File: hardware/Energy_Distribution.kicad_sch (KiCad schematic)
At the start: 22 parts, among them J15 53398-0271, J16 53398-0671, J17 53398-0671, J18 53398-0271, U17 NVTFS5116PLTAG, U18 NVTFS5116PLTAG, U21 LMV321RIYLT, U39 NVTFS5116PLTAG, U4 INA199C1DCKR, U40 NVTFS5116PLTAG

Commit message: commit
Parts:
- removed R32: 110k, symbol Device:R_US
- removed R33, R35: 0.0R, symbol Device:R_US
- removed R34: 37.4k, symbol Device:R_US
- added R75: 110k, footprints:CRCW0603110KFKEAHP, symbol CRCW0603110KFKEAHP:CRCW0603110KFKEAHP
- added R76, R77: 0.0R, footprints:CRCW06030000Z0EAHP, symbol CRCW06030000Z0EAHP:CRCW06030000Z0EAHP
- added R86: 37.4k, footprints:CRCW060337K4FKEAHP, symbol CRCW060337K4FKEAHP:CRCW060337K4FKEAHP
- R29: footprint (none) -> footprints:CRCW060324K0FKEAHP; symbol Device:R_US -> CRCW060324K0FKEAHP:RES
- R30: footprint (none) -> footprints:CRCW06037K50FKEAHP; symbol Device:R_US -> CRCW06037K50FKEAHP:CRCW06037K50FKEAHP; automotive (none) -> Yes; automotive grade (none) -> Grade 0; category (none) -> Res; composition (none) -> Thick Film; device class L1 (none) -> Passive Components; device class L2 (none) -> Resistors; device class L3 (none) -> Chip SMD Resistors; height (none) -> 0.55mm; ipc land pattern name (none) -> RESC16085X45; lead free (none) -> Yes; library id (none) -> ac0eb7131481e5d0; manufacturer (none) -> Vishay; package (none) -> 0603; power (none) -> 250mW; power rating (none) -> 0.33W; resistance (none) -> 7.5kΩ; rohs (none) -> Yes; series (none) -> CRCW-HP e3; temperature coefficient (none) -> 100ppm/°C; temperature range high (none) -> +155°C; temperature range low (none) -> -55°C; tolerance (none) -> 1%; voltage rating (none) -> 75V
- R300: footprint (none) -> footprints:WSL20108L000FEA18; symbol Device:R_US -> WSL20108L000FEA18:WSL20108L000FEA18
- R305: footprint (none) -> footprints:CRCW0603100KFKEAHP; symbol Device:R_US -> CRCW0603100KFKEAHP:CRCW0603100KFKEAHP; Arrow Part Number (none) -> CRCW0603100KFKEAHP; Arrow Price/Stock (none) -> https://www.arrow.com/en/products/crcw0603100kfkeahp/vishay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; Height (none) -> 0.55; Manufacturer_Name (none) -> Vishay; Manufacturer_Part_Number (none) -> CRCW0603100KFKEAHP; Mouser Part Number (none) -> 71-CRCW0603100KFKEAH; Mouser Price/Stock (none) -> https://www.mouser.co.uk/ProductDetail/Vishay-Dale/CRCW0603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
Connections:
- net BC_VFB: now also R76.2, R86.2
- net GND: now also R30.1, R305.1, R77.2; no longer R30.2, R305.2
- net VBAT: now also R300.1, R75.2; no longer R300.2
- net VBUS: now also R29.2; no longer R29.1
- net at C3.1, U17.1, U17.2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: now also R300.2; no longer R300.1
- net at J16.5, J16.6: now also R305.2; no longer R305.1
- new net: R77.1, R86.1
- new net: R29.1, R30.2, U21.3 (+)
- new net: R75.1, R76.1
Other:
- moved on the sheet: R29, R30, R300, R305

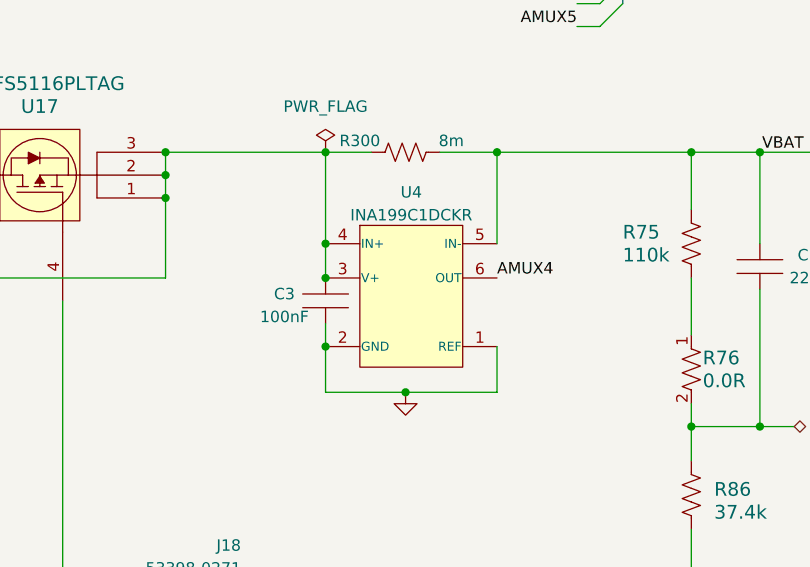
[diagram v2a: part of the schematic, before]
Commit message: hardware: Updating some footprints and 3D models.
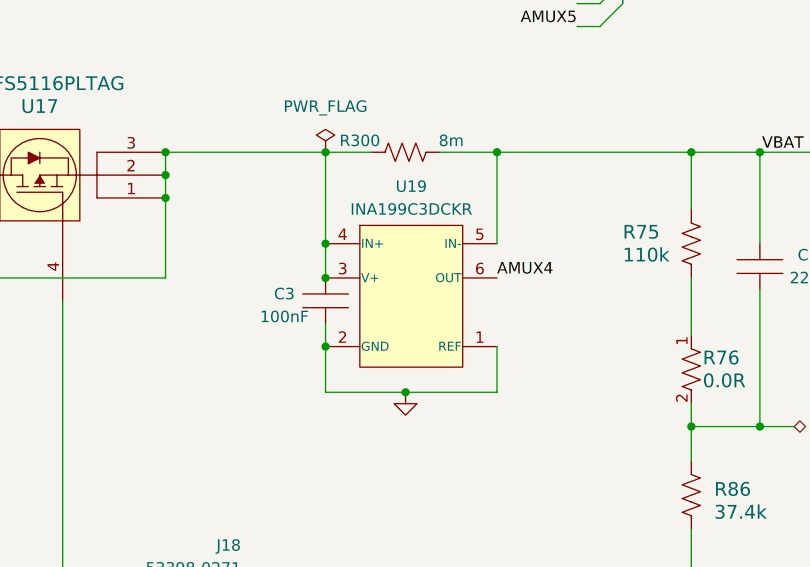
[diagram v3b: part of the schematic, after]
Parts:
- removed U4: INA199C1DCKR, footprints:INA199C1DCKR, symbol INA199C1DCKR:INA199xxDCK
- added U19: INA199C3DCKR, Package_TO_SOT_SMD:SOT-363_SC-70-6, symbol INA199C3DCKR:INA199xxDCK
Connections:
- net AMUX4: now also U19.6 (OUT)
- net GND: now also U19.1 (REF), U19.2 (GND)
- net VBAT: now also U19.5 (IN-)
- net at C3.1, R300.2, U17.1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: now also U19.3 (V+), U19.4 (IN+)
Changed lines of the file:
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@@
   (junction (at 195.58 119.38) (diameter 0) (color 0 0 0 0)
   )
+  (junction (at 213.36 66.04) (diameter 0) (color 0 0 0 0)
+  )
   (junction (at 261.62 74.93) (diameter 0) (color 0 0 0 0)
   )
@@
   (junction (at 81.28 45.72) (diameter 0) (color 0 0 0 0)
   )
-  (junction (at 213.36 66.04) (diameter 0) (color 0 0 0 0)
-  )
   (junction (at 146.05 59.69) (diameter 0) (color 0 0 0 0)
   )
   (junction (at 102.87 62.23) (diameter 0) (color 0 0 0 0)
   )
+  (junction (at 209.55 119.38) (diameter 0) (color 0 0 0 0)
+  )
+  (junction (at 213.36 58.42) (diameter 0) (color 0 0 0 0)
+  )
+  (junction (at 146.05 62.23) (diameter 0) (color 0 0 0 0)
+  )
+  (junction (at 39.37 111.76) (diameter 0) (color 0 0 0 0)
+  )
+  (junction (at 209.55 111.76) (diameter 0) (color 0 0 0 0)
+  )
+  (junction (at 184.15 119.38) (diameter 0) (color 0 0 0 0)
+  )
+  (junction (at 102.87 43.18) (diameter 0) (color 0 0 0 0)
+  )
+  (junction (at 173.99 58.42) (diameter 0) (color 0 0 0 0)
+  )
+  (junction (at 195.58 49.53) (diameter 0) (color 0 0 0 0)
+  )
+  (junction (at 167.64 45.72) (diameter 0) (color 0 0 0 0)
+  )
+  (junction (at 195.58 46.99) (diameter 0) (color 0 0 0 0)
+  )
+  (junction (at 53.34 119.38) (diameter 0) (color 0 0 0 0)
+  )
+  (junction (at 254 74.93) (diameter 0) (color 0 0 0 0)
+  )
   (junction (at 213.36 54.61) (diameter 0) (color 0 0 0 0)
-  )
-  (junction (at 209.55 119.38) (diameter 0) (color 0 0 0 0)
-  )
-  (junction (at 146.05 62.23) (diameter 0) (color 0 0 0 0)
-  )
-  (junction (at 39.37 111.76) (diameter 0) (color 0 0 0 0)
-  )
-  (junction (at 209.55 111.76) (diameter 0) (color 0 0 0 0)
-  )
-  (junction (at 184.15 119.38) (diameter 0) (color 0 0 0 0)
-  )
-  (junction (at 213.36 58.42) (diameter 0) (color 0 0 0 0)
-  )
-  (junction (at 102.87 43.18) (diameter 0) (color 0 0 0 0)
-  )
-  (junction (at 173.99 58.42) (diameter 0) (color 0 0 0 0)
-  )
-  (junction (at 195.58 49.53) (diameter 0) (color 0 0 0 0)
-  )
-  (junction (at 167.64 45.72) (diameter 0) (color 0 0 0 0)
-  )
-  (junction (at 195.58 46.99) (diameter 0) (color 0 0 0 0)
-  )
-  (junction (at 53.34 119.38) (diameter 0) (color 0 0 0 0)
-  )
-  (junction (at 254 74.93) (diameter 0) (color 0 0 0 0)
   )
   (junction (at 39.37 119.38) (diameter 0) (color 0 0 0 0)
@@
     (stroke (width 0) (type default))
   )
+  (wire (pts (xy 213.36 54.61) (xy 213.36 58.42))
+    (stroke (width 0) (type default))
+  )
   (wire (pts (xy 102.87 57.15) (xy 102.87 59.69))
     (stroke (width 0) (type default))
@@
     (stroke (width 0) (type default))
   )
-  (wire (pts (xy 213.36 54.61) (xy 213.36 58.42))
-    (stroke (width 0) (type default))
-  )
   (wire (pts (xy 241.3 30.48) (xy 243.84 30.48))
     (stroke (width 0) (type default))
@@
     (stroke (width 0) (type default))
   )
+  (wire (pts (xy 213.36 66.04) (xy 213.36 71.12))
+    (stroke (width 0) (type default))
+  )
   (wire (pts (xy 146.05 43.18) (xy 146.05 57.15))
     (stroke (width 0) (type default))
@@
     (stroke (width 0) (type default))
   )
-  (wire (pts (xy 213.36 71.12) (xy 213.36 66.04))
+  (wire (pts (xy 213.36 63.5) (xy 213.36 66.04))
     (stroke (width 0) (type default))
   )
@@
   )
   (wire (pts (xy 74.93 60.96) (xy 74.93 63.5))
-    (stroke (width 0) (type default))
-  )
-  (wire (pts (xy 213.36 63.5) (xy 213.36 66.04))
     (stroke (width 0) (type default))
   )
@@
     )
   )
+  (symbol (lib_id "INA199C3DCKR:INA199xxDCK") (at 200.66 73.66 0) (unit 1)
+    (in_bom yes) (on_board yes) (dnp no) (fields_autoplaced)
+    (property "Reference" "U19" (at 222.885 48.26 0)
+      (effects (font (size 1.27 1.27)))
+    )
+    (property "Value" "INA199C3DCKR" (at 222.885 50.8 0)
+      (effects (font (size 1.27 1.27)))
+    )
+    (property "Footprint" "Package_TO_SOT_SMD:SOT-363_SC-70-6" (at 224.282 72.898 0)
+      (effects (font (size 1.27 1.27)) hide)
+    )
+    (property "Datasheet" "http://www.ti.com/lit/ds/symlink/ina199.pdf" (at 223.266 75.184 0)
+      (effects (font (size 1.27 1.27)) hide)
+    )
+    (pin "1")
+    (pin "2")
+    (pin "3")
+    (pin "4")
+    (pin "5")
+    (pin "6")
+    (instances
+      (project "eps-re_project"
+        (path "/2eebaa11-d7ed-4bfd-bc8e-988f68654d29/fd86ef80-5a59-4dab-8bcd-7bed00669ccc"
+          (reference "U19") (unit 1)
+        )
+      )
+    )
+  )
   (symbol (lib_id "power:GND") (at 204.47 142.24 0) (mirror y) (unit 1)
     (in_bom yes) (on_board yes) (dnp no) (fields_autoplaced)
@@
         )
       )
-    )
-  )
-  (symbol (lib_id "INA199C1DCKR:INA199xxDCK") (at 200.66 73.66 0) (unit 1)
-    (in_bom yes) (on_board yes) (dnp no)
-    (property "Reference" "U4" (at 222.885 48.895 0)
-      (effects (font (size 1.27 1.27)))
-    )
-    (property "Value" "INA199C1DCKR" (at 222.885 51.435 0)
-      (effects (font (size 1.27 1.27)))
-    )
-    (property "Footprint" "footprints:INA199C1DCKR " (at 224.282 72.898 0)
-      (effects (font (size 1.27 1.27)) hide)
-    )
-    (property "Datasheet" "http://www.ti.com/lit/ds/symlink/ina199.pdf" (at 223.266 75.184 0)
-      (effects (font (size 1.27 1.27)) hide)
-    )
-    (pin "1")
-    (pin "2")
-    (pin "3")
-    (pin "4")
-    (pin "5")
-    (pin "6")
-    (instances
-      (project "eps-re_project"
-        (path "/2eebaa11-d7ed-4bfd-bc8e-988f68654d29/b2d6a676-b7d9-423e-8a54-05279452700b"
-          (reference "U4") (unit 1)
-        )
-        (path "/2eebaa11-d7ed-4bfd-bc8e-988f68654d29/4f028e55-4c46-47b6-9c45-f6b50d9d4db8"
-          (reference "U8") (unit 1)
-        )
-        (path "/2eebaa11-d7ed-4bfd-bc8e-988f68654d29/fd86ef80-5a59-4dab-8bcd-7bed00669ccc"
-          (reference "U19") (unit 1)
-        )
-      )
-      (project "EPS Analogico"
-        (path "/9af6272d-3cb8-4e37-b792-5888e300588f"
-          (reference "U1") (unit 1)
-        )
-      )

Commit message: hardware: Updating 3D models, component placement and more.
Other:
- title: (none) -> Reliability Enhanced Electrical Power System
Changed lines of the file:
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@@
 (kicad_sch (version 20230121) (generator eeschema)
   (paper "A4")
+  (title_block
+    (title "Reliability Enhanced Electrical Power System")
+    (date "2023-08-03")
+    (rev "v0.0")
+    (comment 1 "João C. E. Barcellos <joaoclaudiobarcellos@gmail.com>")
+    (comment 2 "Laura Debastiani <laudebastiani@gmail.com>")
+  )
   (junction (at 146.05 57.15) (diameter 0) (color 0 0 0 0)
   )

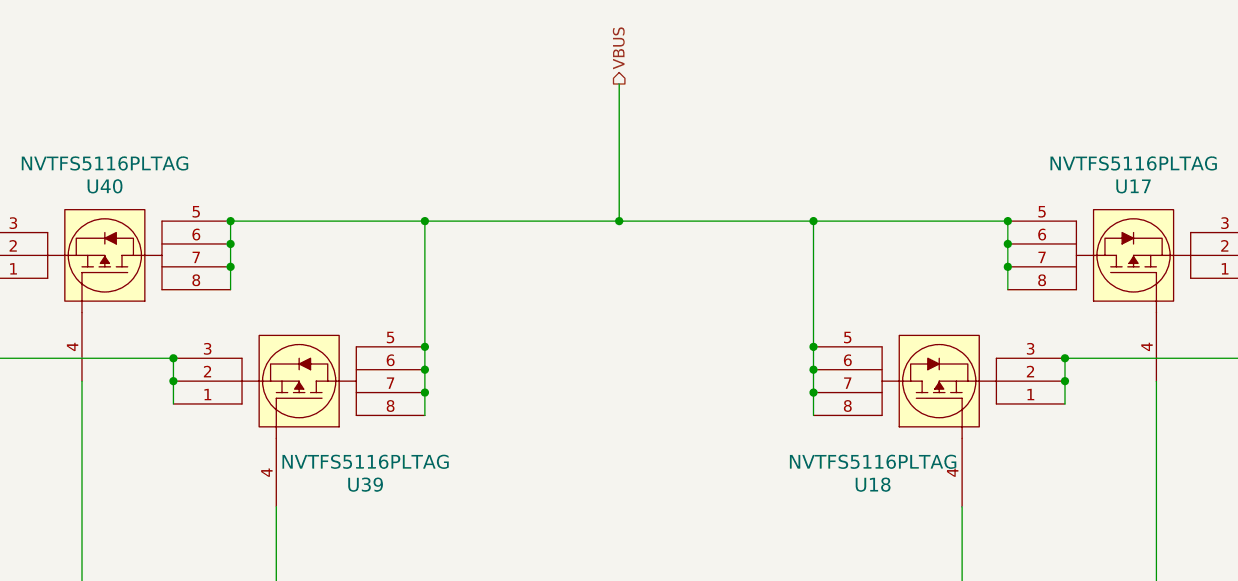
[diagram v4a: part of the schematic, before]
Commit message: hardware: Adding some 3D models, changing the placement of components and routing more nets.
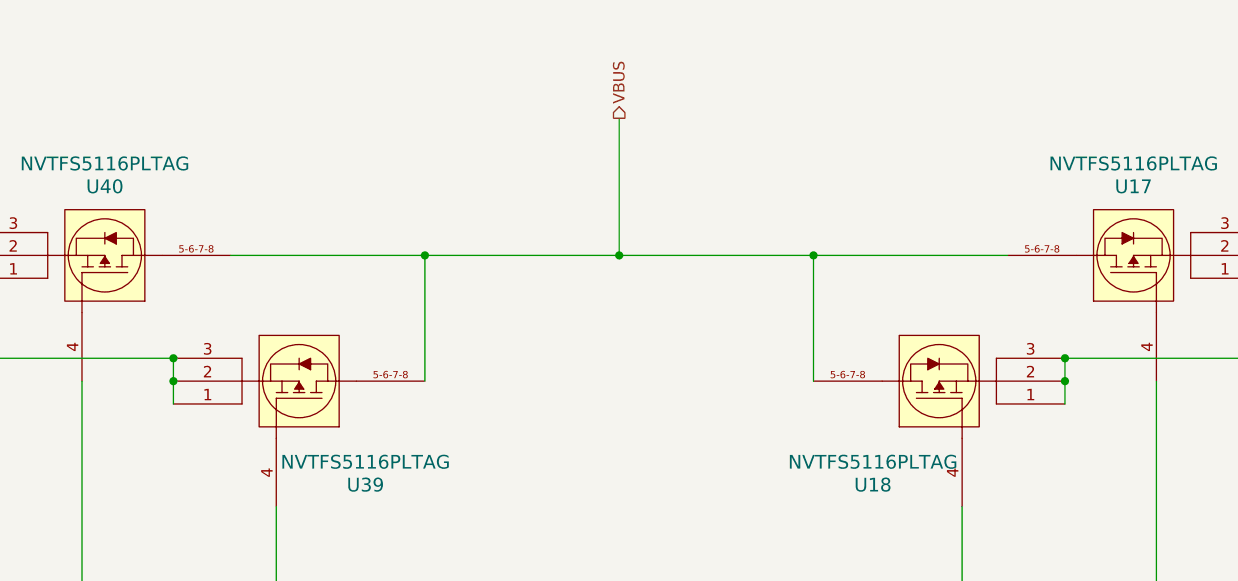
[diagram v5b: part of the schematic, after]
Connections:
- net VBUS: now also U17.5-6-7-8, U18.5-6-7-8, U39.5-6-7-8, U40.5-6-7-8; no longer U17.5, U17.6, U17.7, U17.8, U18.5, U18.6, U18.7, U18.8, U39.5, U39.6, U39.7, U39.8, U40.5, U40.6, U40.7, U40.8

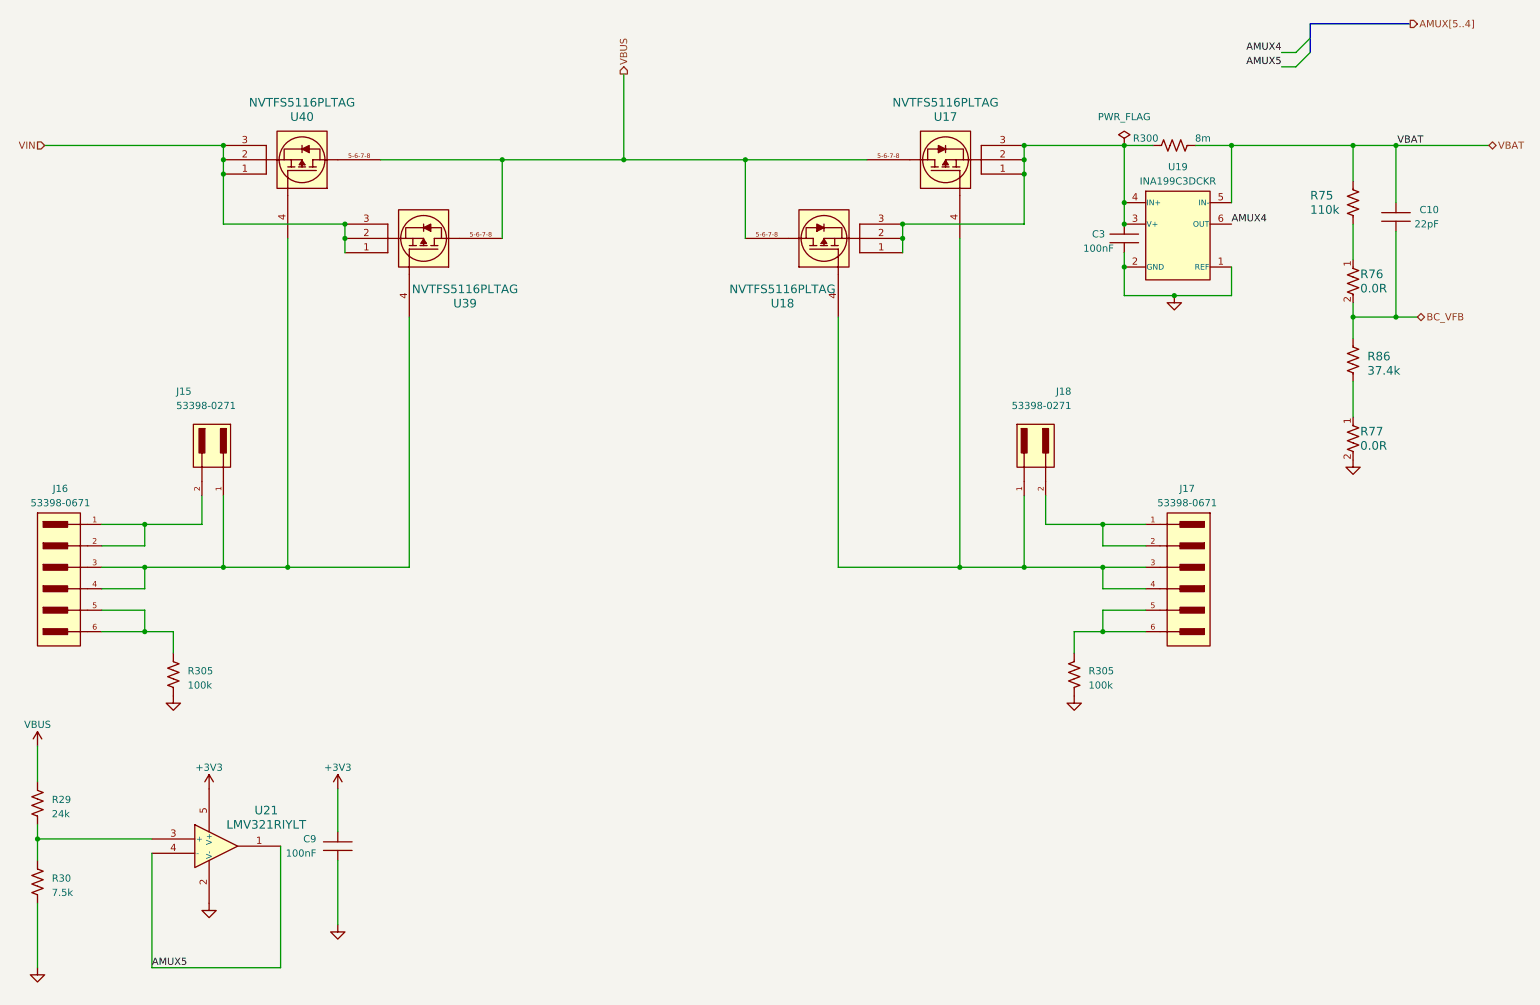
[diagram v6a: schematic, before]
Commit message: hardware: Updating the MPPT circuit.
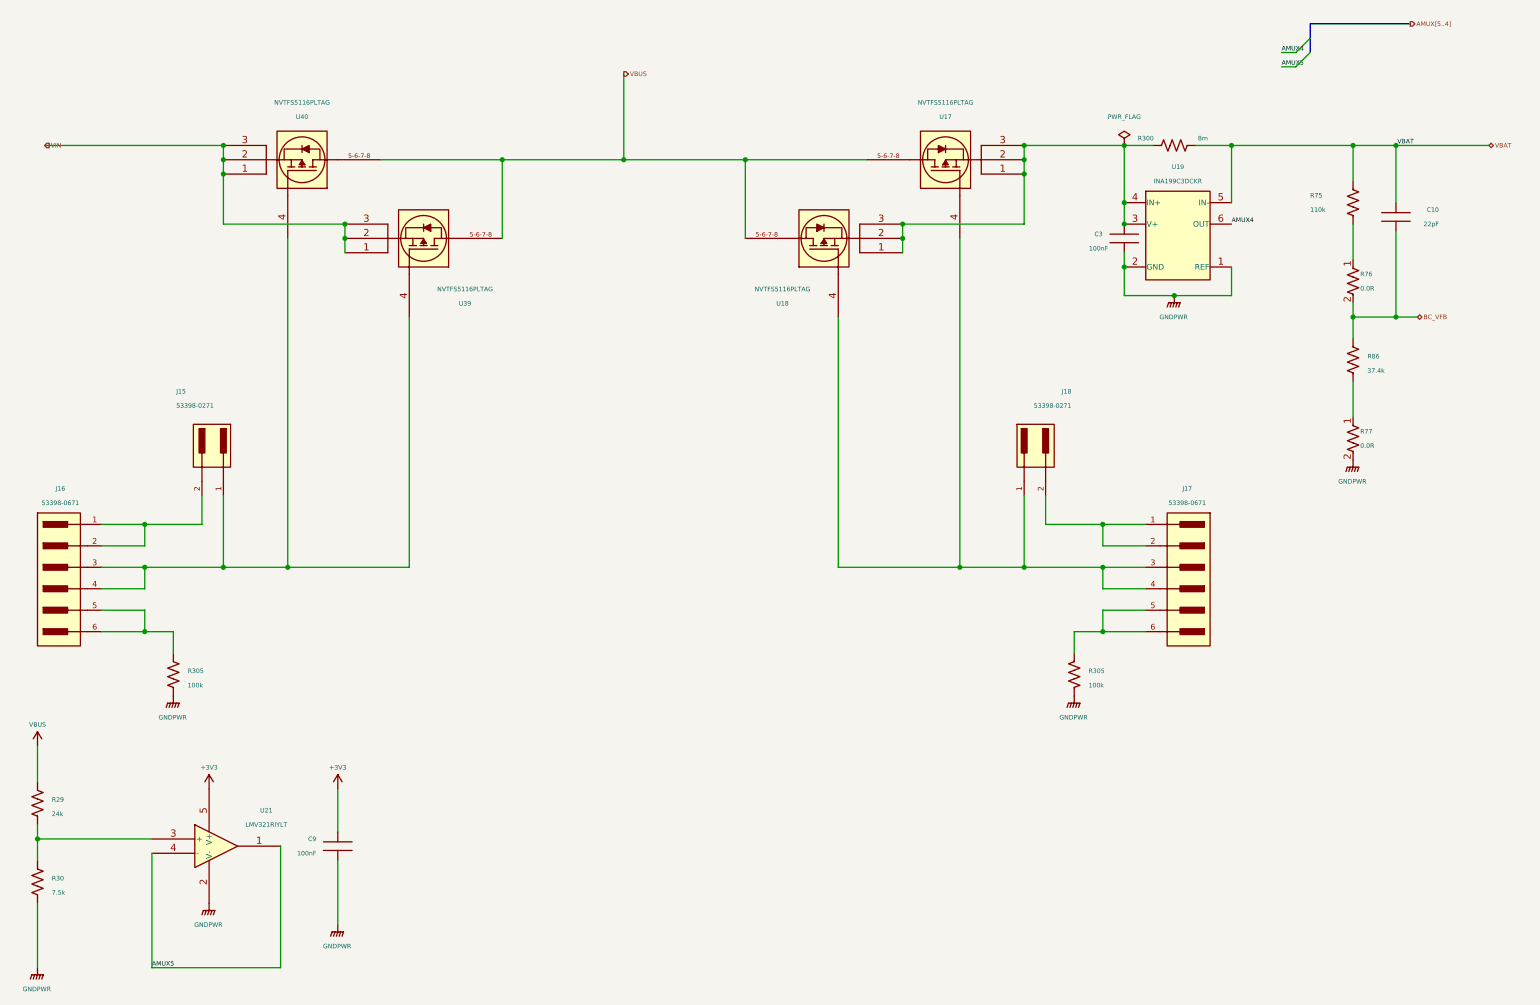
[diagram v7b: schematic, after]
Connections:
- net GND renamed GNDPWR
